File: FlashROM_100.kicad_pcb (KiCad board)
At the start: 2 copper layers, 16.4 x 34.2 mm, 5 parts, among them J1 LH535618 DIP LEGS, U1 29F010

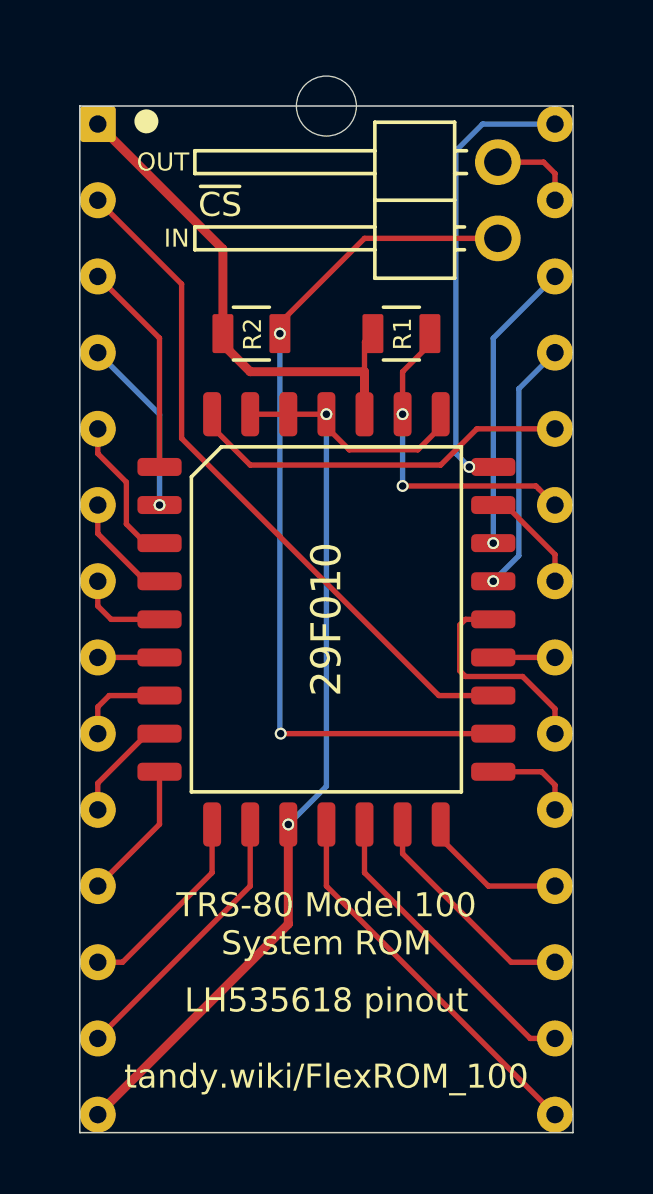
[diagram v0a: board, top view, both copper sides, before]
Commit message: FlexROM_100 & FlashROM_100 fix ALE/WE
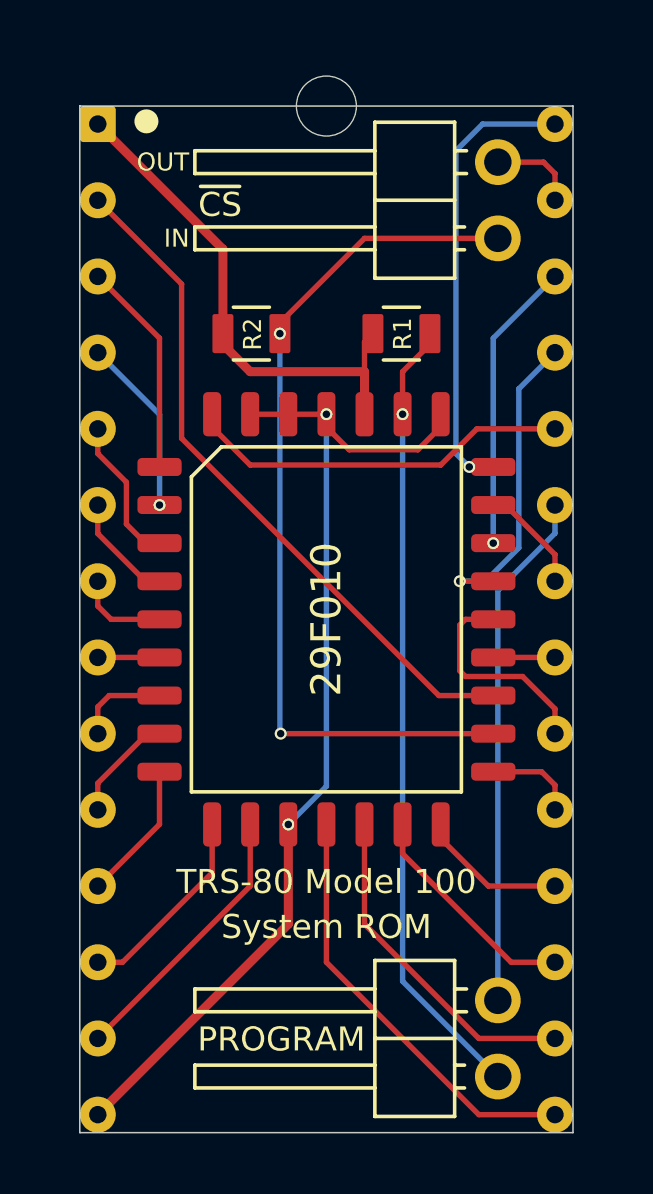
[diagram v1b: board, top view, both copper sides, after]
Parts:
- added JP2: Write-Enable, 000_LOCAL:Pin_Header_Angled_1x02_Pitch2.54mm, F.Cu at (155.7, 115.2)
- JP1: value ~CS~ breakout (REX TP1) -> ~CS~ breakout
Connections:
- J1 pad 23: /~WE -> /ALE
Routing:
- net /ALE: track 0.00 -> 17.3 mm
- net /~WE: track 10.8 -> 26.5 mm, vias 2 -> 1
- net /A9: track 8.47 -> 10.6 mm
- net /D3: track 12.8 -> 14.3 mm
- net /D4: track 10.2 -> 11.3 mm
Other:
- board text added: "PROGRAM"
- board text removed: "LH535618 pinout"

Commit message: simpler programming adapters, update pics and BOMs
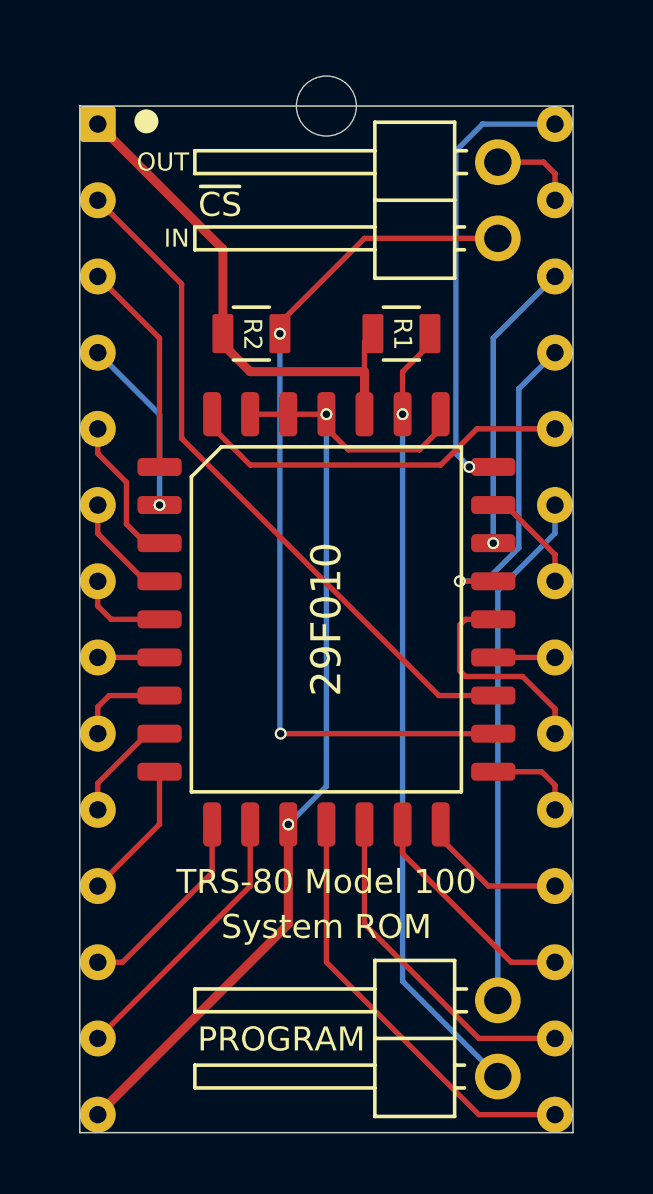
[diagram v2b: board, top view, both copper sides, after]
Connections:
- net /ALE renamed /ALE_~WE
- net /~CS_IN renamed /~CS
- net /~CS_OUT renamed /~CS_BUS

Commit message: add FlashROM_100_tsop
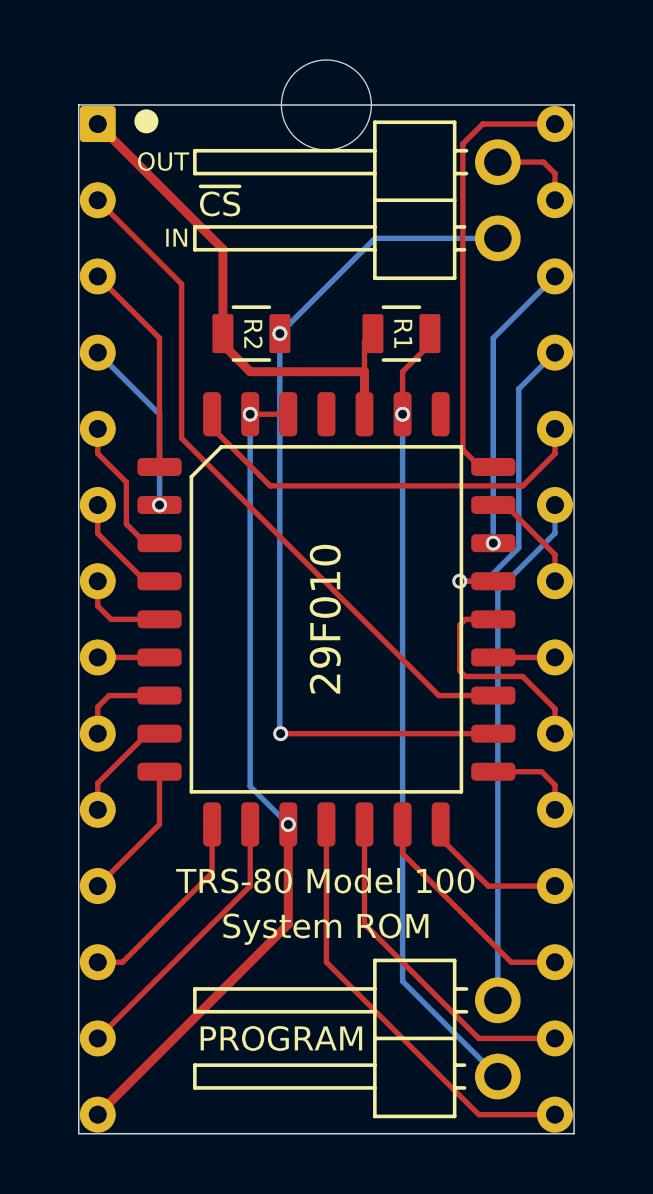
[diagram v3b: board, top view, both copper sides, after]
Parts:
- added REF**: NPTH_3mm, 000_LOCAL:NPTH_3mm, F.Cu at (150.0, 82.9)
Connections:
- U1 pad 1: GND -> (no net)
- U1 pad 30: GND -> (no net)
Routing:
- net GND: track 34.4 -> 27.8 mm
- net /A12: track 12.9 -> 14.0 mm
- net /A14: track 15.2 -> 14.8 mm, vias 1 -> 0
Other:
- board size 16.4 x 34.2 mm -> 16.5 x 34.3 mm
- net class Default: via_dia 0.4 -> 0.5; via_drill 0.25 -> 0.3
- rule via_min_drill: 0.25 -> 0.3
- rule via_min_size: 0.4 -> 0.5
